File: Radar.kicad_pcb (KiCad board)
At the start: 2 copper layers, 119 parts, among them J1 Receive_Antenna, J10 Conn_Coaxial, J11 Conn_02x05_Counter_Clockwise, J2 VCO_Tune, J3 Transmit Antenna, J4 Output, J5 Conn_Coaxial, J6 Conn_Coaxial, J7 Conn_Coaxial, J8 Conn_Coaxial, J9 Conn_Coaxial, U10 AD5252, U11 LT1722, U12 AD8039, U13 PMA-63GLN+, U14 QPC6324, U15 PMA-63GLN+, U16 QPC6324, U17 HMC218BMS8GE, U18 AZ1117-5.0, U19 RP117, U20 MIC5317, U21 L78L33_SO8, U23 HMC430, U24 RFPA5542

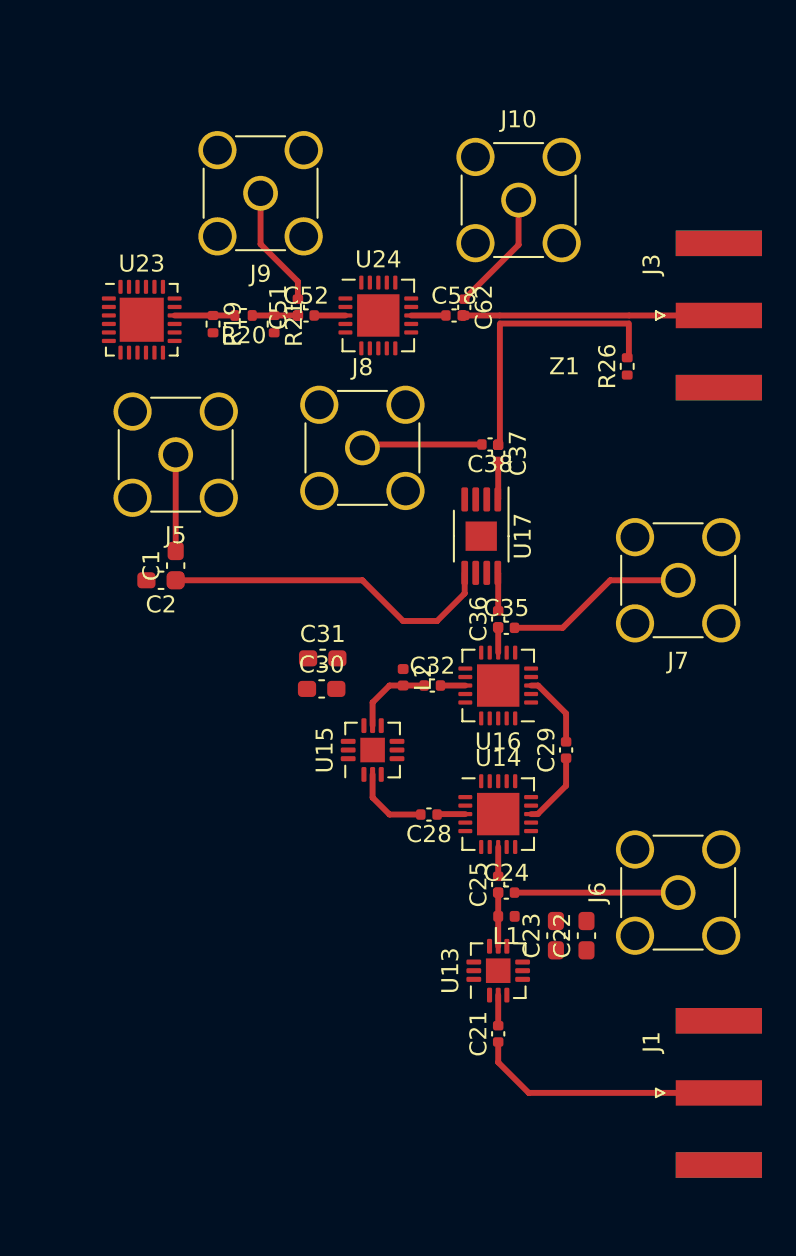
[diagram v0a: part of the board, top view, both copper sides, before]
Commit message: Shrunk the microwave section
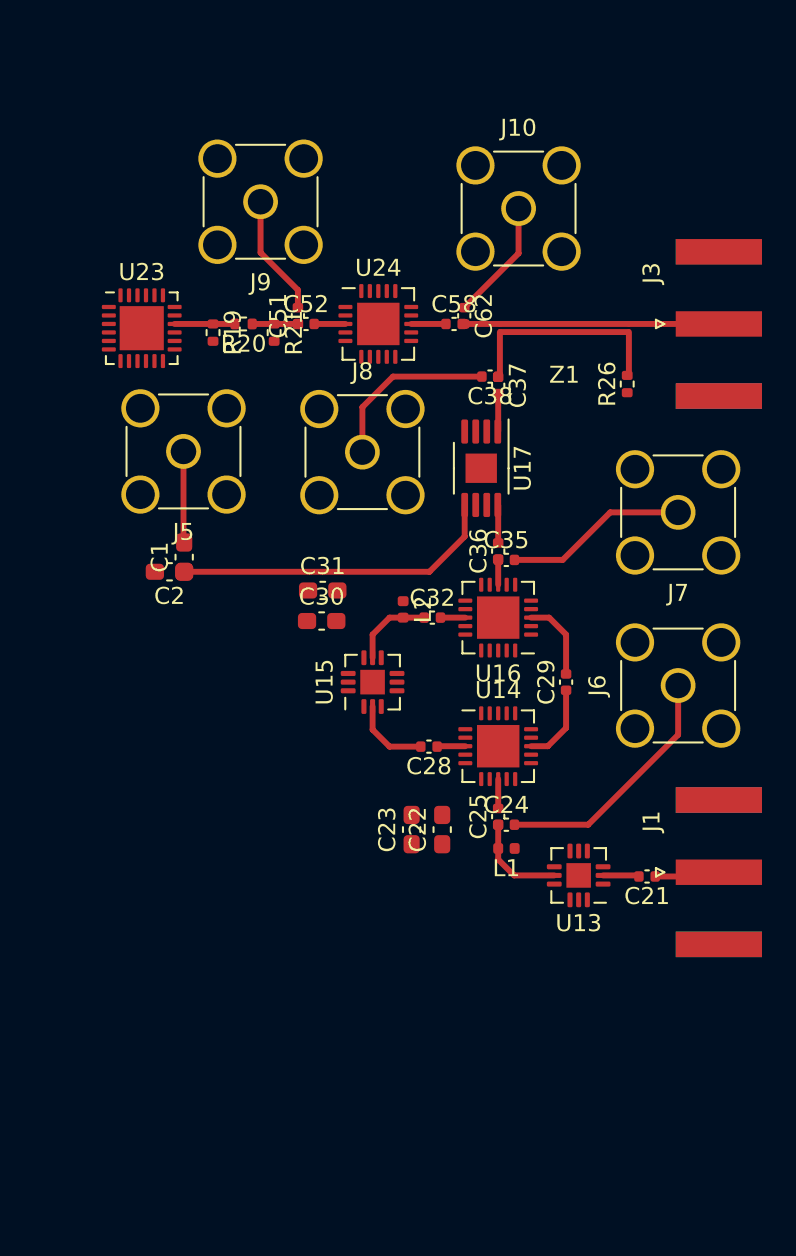
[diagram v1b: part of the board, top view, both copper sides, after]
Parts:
- moved J1 13.0 mm to (175.0, 72.0)
- moved C21 12.8 mm to (170.8, 72.2), turned to 180 degrees
- moved J6 12.2 mm to (172.6, 61.0)
- moved C22 10.6 mm to (158.7, 69.5)
- moved C23 10.6 mm to (156.9, 69.5)
- moved U13 7.35 mm to (166.7, 72.2), turned to 180 degrees
- moved C24 4.00 mm to (162.5, 69.2)
- moved C25 4.00 mm to (162.0, 68.7)
- moved C28 4.00 mm to (157.9, 64.6)
- moved C29 4.00 mm to (166.0, 60.8)
- moved C30 4.00 mm to (151.6, 57.2)
- moved C31 4.00 mm to (151.7, 55.4)
- moved C32 4.00 mm to (158.1, 57.0)
- moved C35 4.00 mm to (162.5, 53.6)
- moved C36 4.00 mm to (162.0, 53.1)
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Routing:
- net /ReceiverRF/RF_IN: track 14.9 -> 3.75 mm
- net Net-(C24-Pad2): track 9.64 -> 14.7 mm
- net /ReceiverRF/LO_IN: track 7.21 -> 2.89 mm
- net Net-(C38-Pad2): track 7.12 -> 10.4 mm
- net Net-(C24-Pad1): track 3.16 -> 5.74 mm
- net Net-(R26-Pad2): track 2.06 -> 2.60 mm

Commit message: Curved tracks
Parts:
- removed C24, C35, C38, C51: DNP, Capacitor_SMD:C_0402_1005Metric
- removed C25, C36, C37, C52, C58, C62: 100pF, Capacitor_SMD:C_0402_1005Metric
- added CJ1: 100pF, own:0402_Jumper_Tapered, F.Cu at (162.0, 70.2)
- added CJ2: 100pF, own:0402_Jumper_Tapered, F.Cu at (162.0, 53.4)
- added CJ3: 100pF, own:0402_Jumper_Tapered, F.Cu at (162.0, 42.8)
- added CJ4: 100pF, own:0402_Jumper_Tapered, F.Cu at (150.8, 39.6)
- added CJ5: 100pF, own:0402_Jumper_Tapered, F.Cu at (160.2, 39.6)
- C21, C28, C29, C32: footprint Capacitor_SMD:C_0402_1005Metric -> own:0402_Tapered
- R26: footprint Resistor_SMD:R_0402_1005Metric -> own:0402_Tapered
- moved C22 10.1 mm to (163.7, 78.3)
- moved C23 10.1 mm to (161.9, 78.3)
- moved L1 4.92 mm to (164.0, 75.3), turned to 90 degrees
- moved L2 3.53 mm to (154.1, 59.2), turned to 0 degrees
- moved J9 3.20 mm to (144.8, 32.6)
- moved J10 2.82 mm to (166.0, 32.6)
- moved C31 2.64 mm to (149.7, 57.2)
- moved U13 2.61 mm to (166.7, 74.8)
- moved J1 2.60 mm to (175.0, 74.6)
- moved C21 2.59 mm to (171.2, 74.8), turned to 0 degrees
- moved C30 2.46 mm to (149.7, 58.8)
- moved U15 1.16 mm to (154.6, 62.0)
- moved C28 1.04 mm to (158.2, 65.6), turned to 0 degrees
- moved U14 1.02 mm to (162.0, 65.6)
- moved R26 1.01 mm to (169.8, 44.2), turned to 270 degrees
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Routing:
- net Net-(C1-Pad2): track 5.38 -> 0.00 mm
- net Net-(CJ5-Pad3): track 7.17 -> 10.5 mm
- net Net-(CJ4-Pad3): track 7.15 -> 9.88 mm
- net Net-(C28-Pad2): track 4.62 -> 3.06 mm
- net Net-(CJ1-Pad1): track 5.74 -> 7.27 mm
- net Net-(C32-Pad1): track 4.82 -> 5.63 mm
- net /Transmitter/RF_OUT: track 6.10 -> 5.30 mm
- net Net-(R19-Pad1): track 3.55 -> 2.95 mm
- net Net-(C29-Pad1): track 4.73 -> 5.33 mm
- net Net-(R26-Pad2): track 2.60 -> 3.17 mm
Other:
- net class Default: clearance 0.1 -> 0.09
- net class RF: clearance 0.1 -> 0.09
- rule trace_clearance: 0.1 -> 0.09

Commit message: Fixed connector
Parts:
- J11: value Conn_02x05_Counter_Clockwise -> Conn_02x05_Odd_Even
- moved J11 3.82 mm to (106.0, 81.0)
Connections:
- J11 pad 1: +6V -> GND
- J11 pad 10: -5V -> /Connector/PA_EN
- J11 pad 2: GND -> -5V
- J11 pad 3: /Connector/PA_EN -> +6V
- J11 pad 4: /Connector/SW_CTR1 -> /Connector/SDA
- J11 pad 5: /Connector/SW_CTR2 -> /Connector/SW_CTR1
- J11 pad 6: /Connector/PDET -> /Connector/SCL
- J11 pad 7: /Connector/SCL -> /Connector/SW_CTR2
- J11 pad 8: /Connector/SDA -> /Connector/PDET

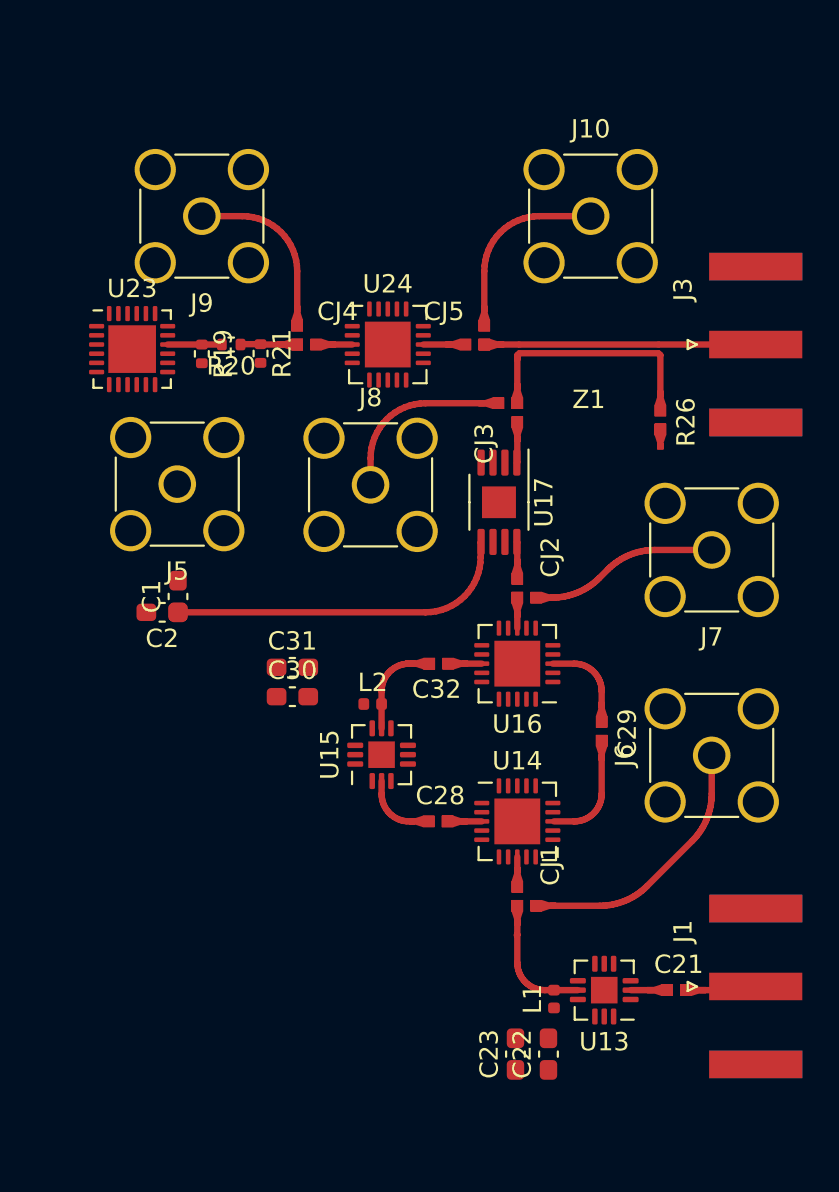
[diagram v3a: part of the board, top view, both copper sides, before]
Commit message: Moved test points
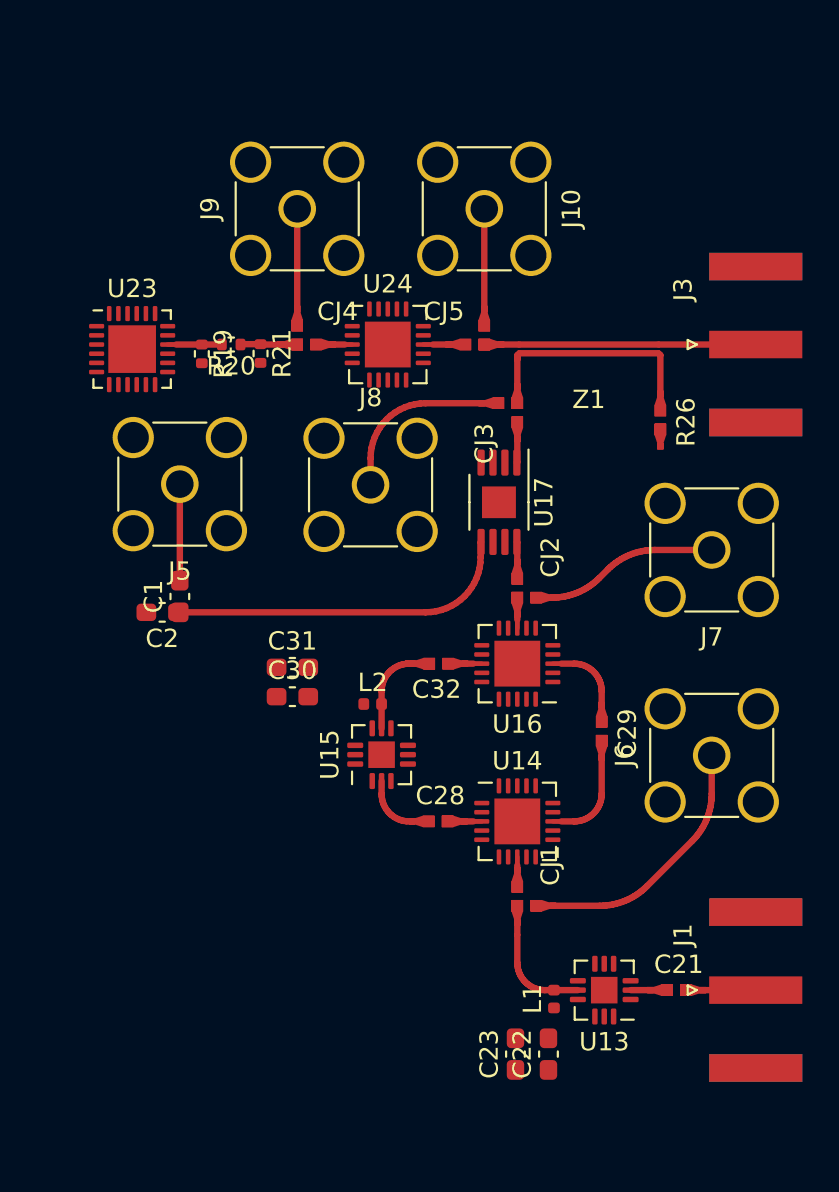
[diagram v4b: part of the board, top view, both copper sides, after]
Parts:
- moved J10 5.81 mm to (160.2, 32.2), turned to 270 degrees
- moved J9 5.22 mm to (150.0, 32.2), turned to 90 degrees
- moved J1 0.20 mm to (175.0, 74.8)
- moved J5 0.14 mm to (143.6, 47.2)
- moved C1 0.10 mm to (143.6, 53.3)
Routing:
- net Net-(C1-Pad2): track 0.00 -> 5.27 mm
- net Net-(CJ5-Pad3): track 10.5 -> 6.37 mm
- net Net-(CJ4-Pad3): track 9.88 -> 6.37 mm
- net Net-(C28-Pad1): track 1.86 -> 2.78 mm

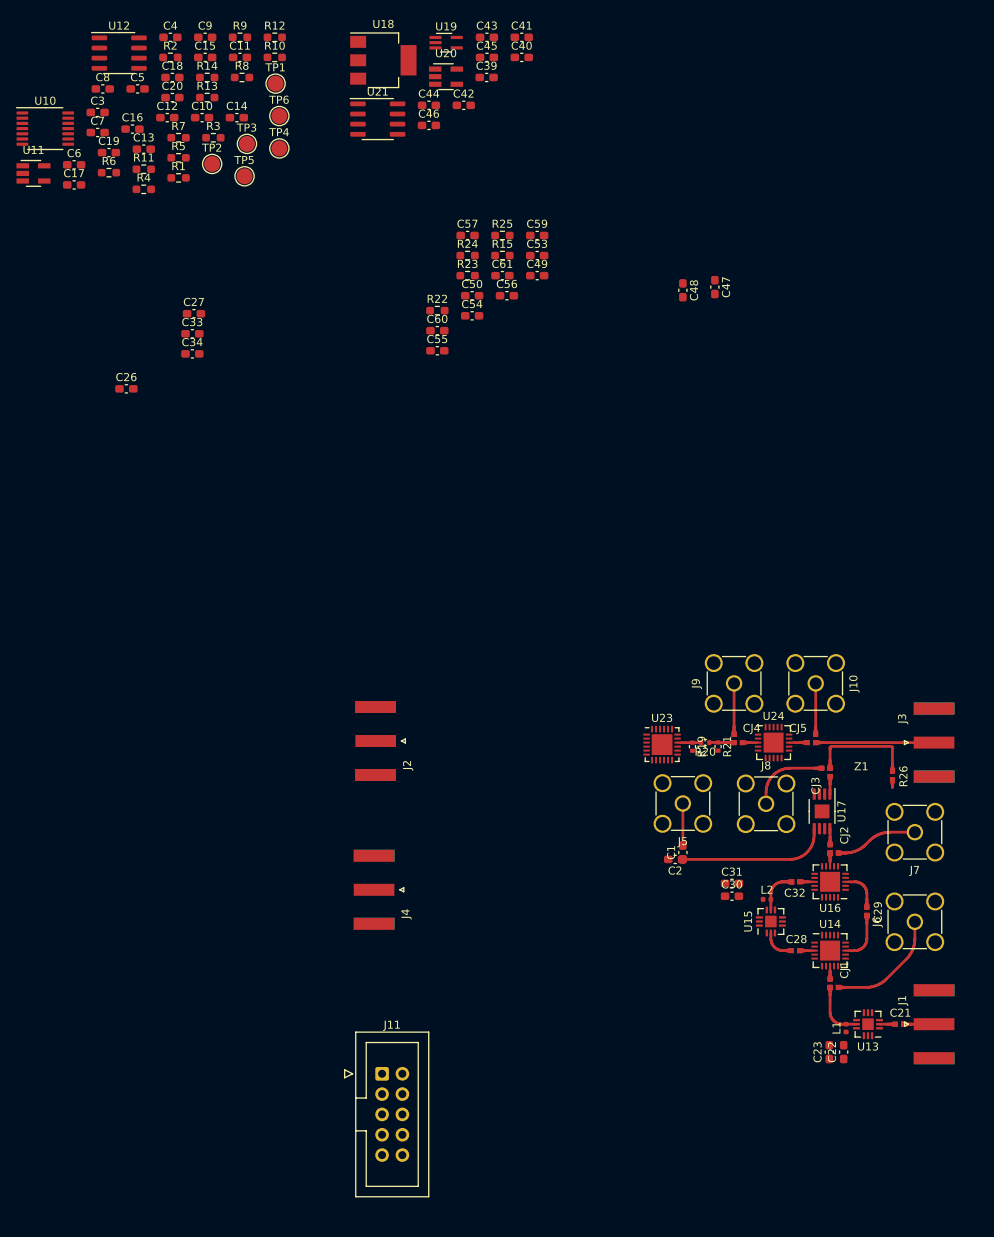
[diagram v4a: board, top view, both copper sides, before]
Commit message: IF and power layout mostly finished
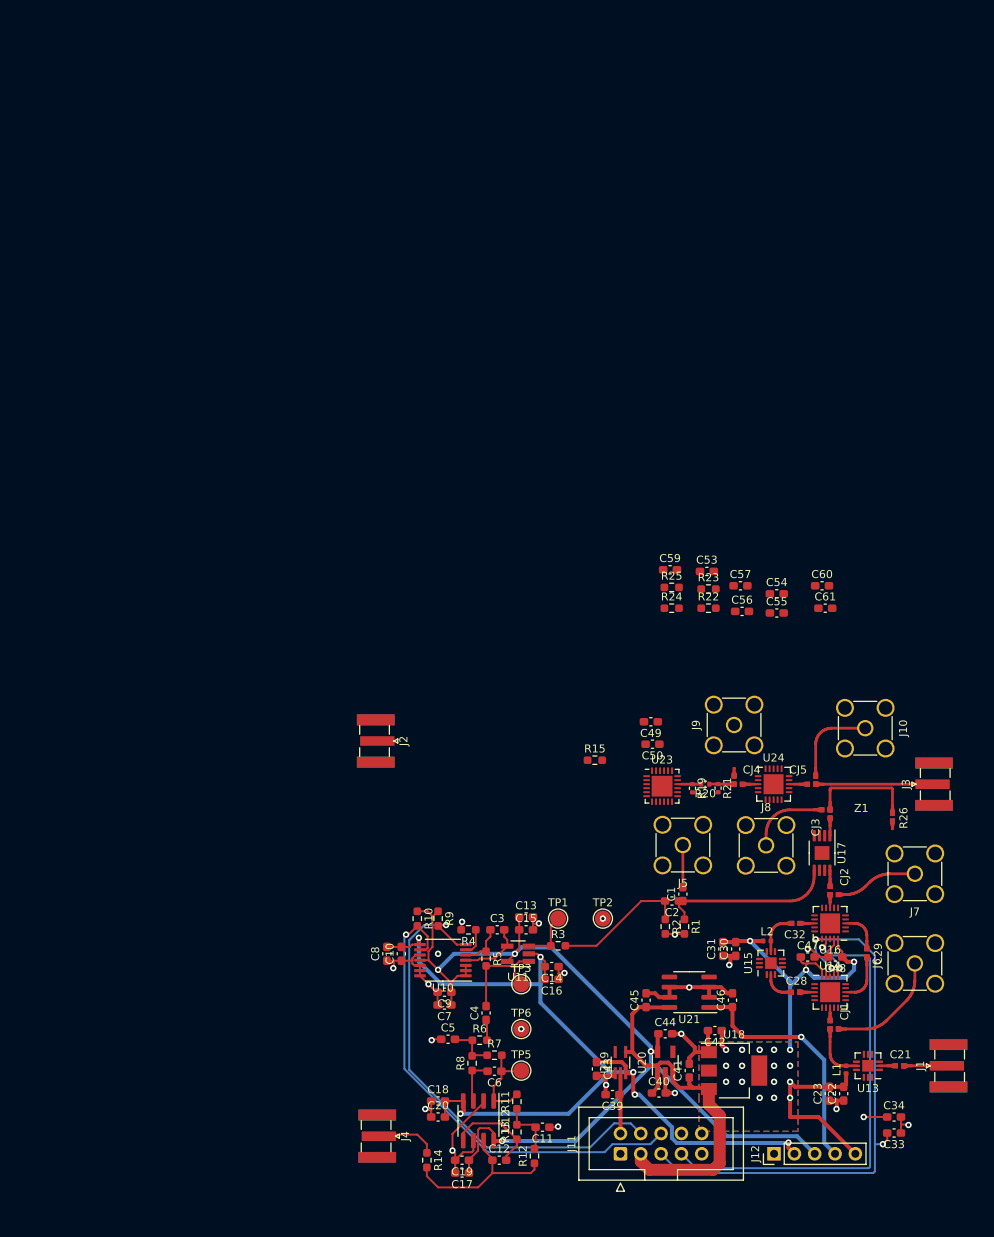
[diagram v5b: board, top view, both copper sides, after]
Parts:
- removed C26, C27: 220pF, Capacitor_SMD:C_0603_1608Metric_Pad1.08x0.95mm_HandSolder
- removed TP4: TP, TestPoint:TestPoint_Pad_D2.0mm
- added J12: supply rails, Connector_PinHeader_2.54mm:PinHeader_1x05_P2.54mm_Vertical, F.Cu at (155.0, 91.0)
- J1, J2, J3, J4: footprint Connector_Coaxial:SMA_Amphenol_132289_EdgeMount -> own:SMA_ADAM_TECH_edge_mount
- J10, J5, J6, J7, J8, J9: footprint Connector_Coaxial:SMA_Amphenol_901-144_Vertical -> Connector_Coaxial:SMA_Amphenol_132134-11_Vertical
- moved R12 143.6 mm to (125.0, 91.3), turned to 90 degrees
- moved U12 140.8 mm to (118.0, 86.9), turned to 270 degrees
- moved C11 139.0 mm to (126.0, 87.7), turned to 180 degrees
- moved R14 138.1 mm to (111.6, 91.8), turned to 270 degrees
- moved C12 136.8 mm to (120.7, 91.8)
- moved R13 135.0 mm to (122.8, 88.3), turned to 90 degrees
- moved U18 133.7 mm to (150.0, 80.6)
- moved C19 133.5 mm to (116.0, 91.8), turned to 180 degrees
- moved C33 132.9 mm to (170.0, 88.4), turned to 180 degrees
- moved C17 132.7 mm to (116.0, 93.4), turned to 180 degrees
- moved C18 132.2 mm to (113.0, 84.4)
- moved C20 131.7 mm to (113.0, 86.4)
- moved C41 130.8 mm to (144.4, 80.6), turned to 90 degrees
- moved C40 130.6 mm to (140.6, 83.4)
- moved C43 129.7 mm to (132.8, 80.4), turned to 270 degrees
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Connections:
- U21 pad 4: (no net) -> Net-(U21-Pad4)
- U21 pad 5: (no net) -> Net-(U21-Pad5)
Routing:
- net +2V5: track 0.00 -> 122.5 mm, vias 0 -> 4
- net -2V5: track 0.00 -> 110.4 mm, vias 0 -> 6
- net GND: track 0.00 -> 92.3 mm, vias 0 -> 21
- net /Connector/SW_CTR1: track 0.00 -> 72.1 mm, vias 0 -> 3
- net +5V: track 0.00 -> 66.8 mm, vias 0 -> 19
- net /Connector/SW_CTR2: track 0.00 -> 65.2 mm, vias 0 -> 3
- net /Connector/SDA: track 0.00 -> 61.8 mm, vias 0 -> 1
- net /Connector/SCL: track 0.00 -> 60.4 mm, vias 0 -> 1
- net +6V: track 0.00 -> 50.1 mm
- net +3V3: track 0.00 -> 30.8 mm, vias 0 -> 1
- net Net-(C12-Pad1): track 0.00 -> 21.3 mm
- net Net-(C2-Pad2): track 0.00 -> 17.1 mm
- net Net-(C4-Pad2): track 0.00 -> 13.2 mm
- net Net-(C12-Pad2): track 0.00 -> 12.2 mm
- net Net-(C6-Pad1): track 0.00 -> 11.9 mm
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- added copper zone on B.Cu, net +5V
- added copper zone on F.Cu, net +5V
- added copper zone on In1.Cu, net GND
- added copper zone on In2.Cu, net GND
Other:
- copper layers 2 -> 4
